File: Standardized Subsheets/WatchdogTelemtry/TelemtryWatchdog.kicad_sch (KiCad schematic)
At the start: 1 part

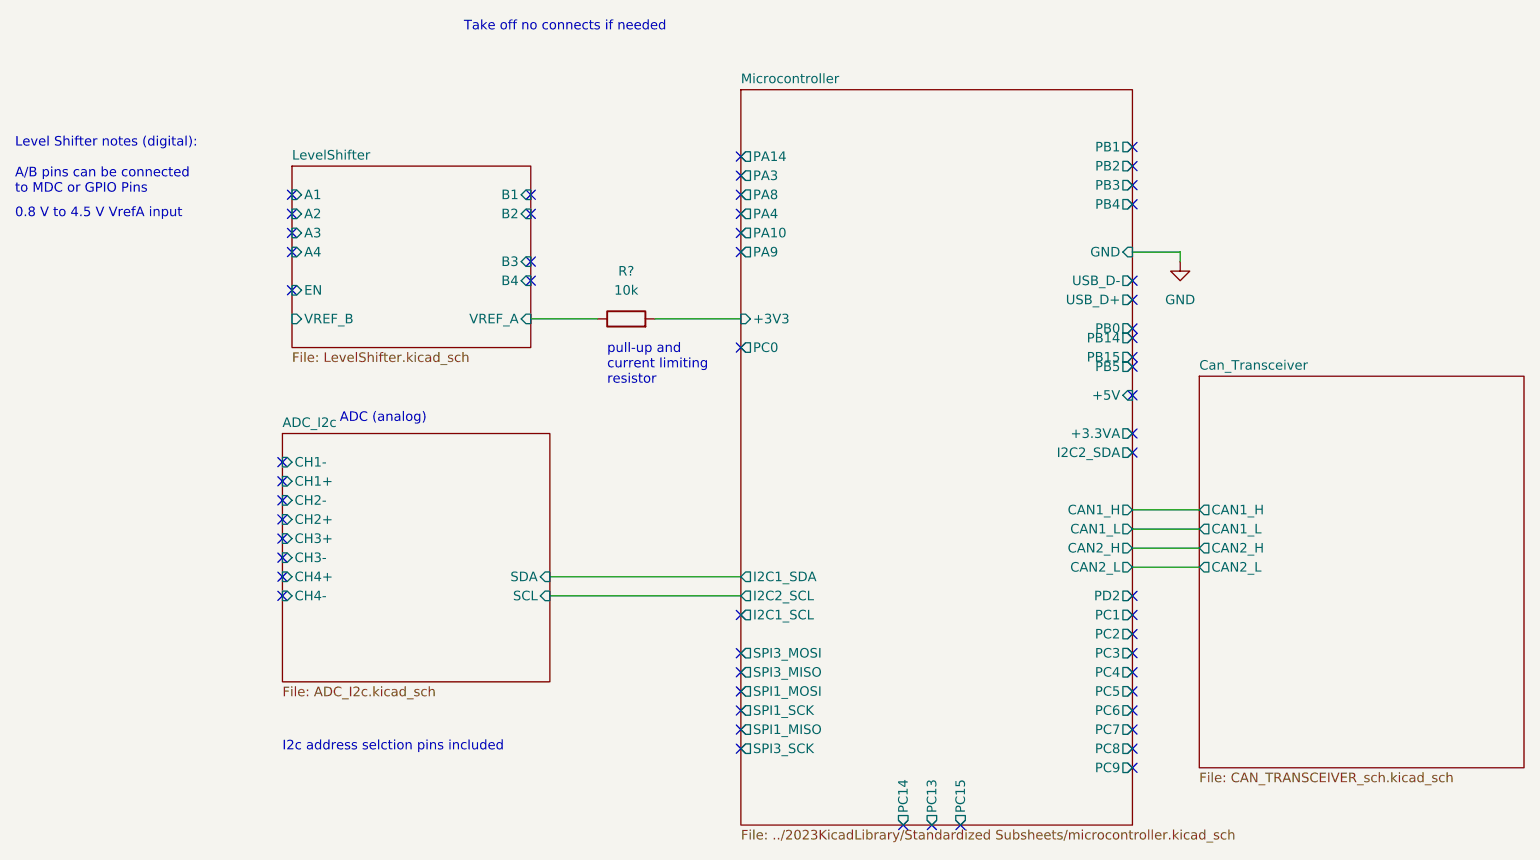
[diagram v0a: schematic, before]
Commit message: adding watchdog
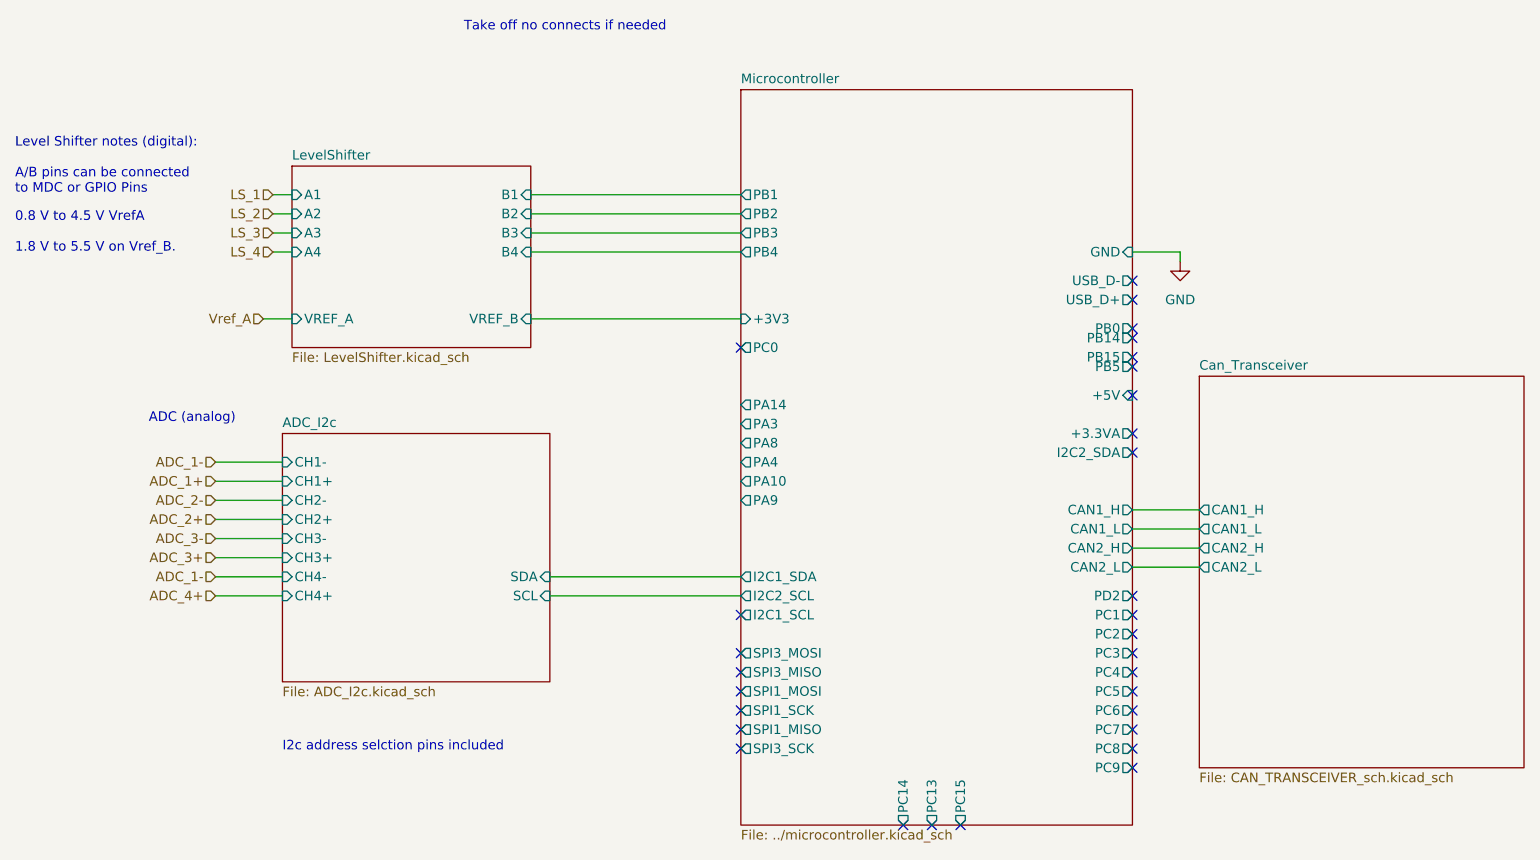
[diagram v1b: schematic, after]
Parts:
- removed R?: 10k, symbol Device:R
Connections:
- no-connect marks 57 -> 30
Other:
- sheet LevelShifter ports: added none; removed EN
- sheet Microcontroller: file ../2023KicadLibrary/Standardized Subsheets/microcontroller.kicad_sch -> ../microcontroller.kicad_sch
- note added: "0.8 V to 4.5 V VrefA 1.8 V to 5.5 V on Vref_B."
- note removed: "0.8 V to 4.5 V VrefA input"
- note removed: "pull-up and current limiting resistor"

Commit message: added new watchdog schematic
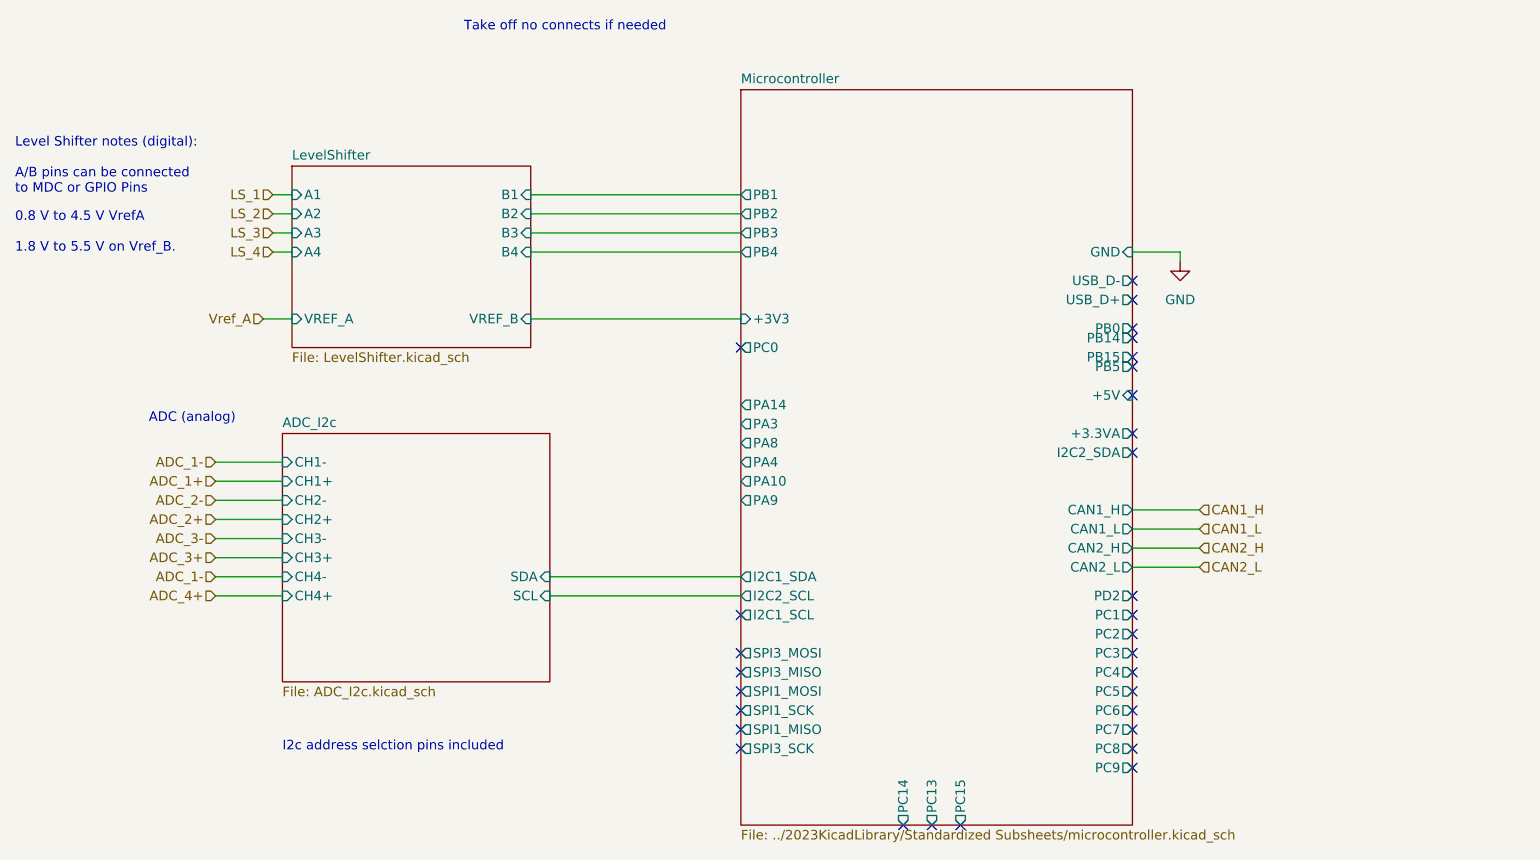
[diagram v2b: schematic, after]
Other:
- removed sheet Can_Transceiver
- sheet Microcontroller: file ../microcontroller.kicad_sch -> ../2023KicadLibrary/Standardized Subsheets/microcontroller.kicad_sch
